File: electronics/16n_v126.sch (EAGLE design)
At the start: 112 parts, among them J1 PJ302M, J10 PJ302M, J11 PJ302M, J12 PJ302M, J13 PJ302M, J14 PJ302M, J15 PJ302M, J16 PJ302M, J2 PJ302M, J3 PJ302M, J4 PJ302M, J5 PJ302M, J6 PJ302M, J7 PJ302M, J8 PJ302M, J9 PJ302M, U1 CD74HC4067SM96, U2 MCP6004_SMD, U3 MCP6004_SMD, U4 MCP6004_SMD, U5 MCP6004_SMD, U6 MCP6004_SMD, U7 MCP6004_SMD, U8 MCP6004_SMD, U9 MCP6004

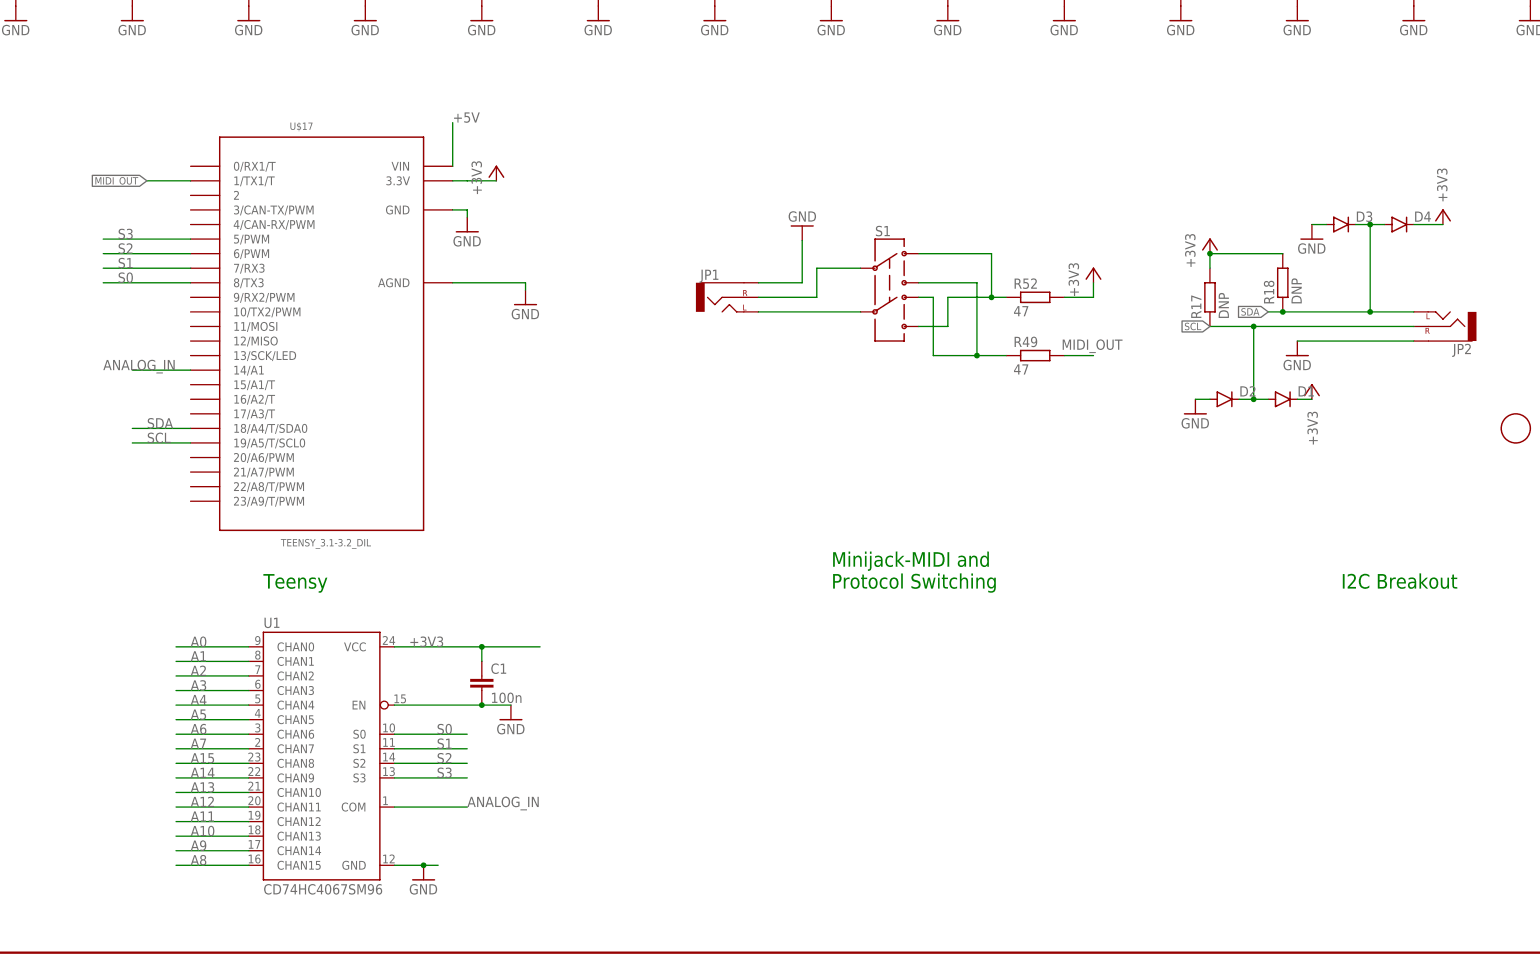
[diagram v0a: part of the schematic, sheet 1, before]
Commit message: 1.26 gets its own files. 1.31 is now the main version.
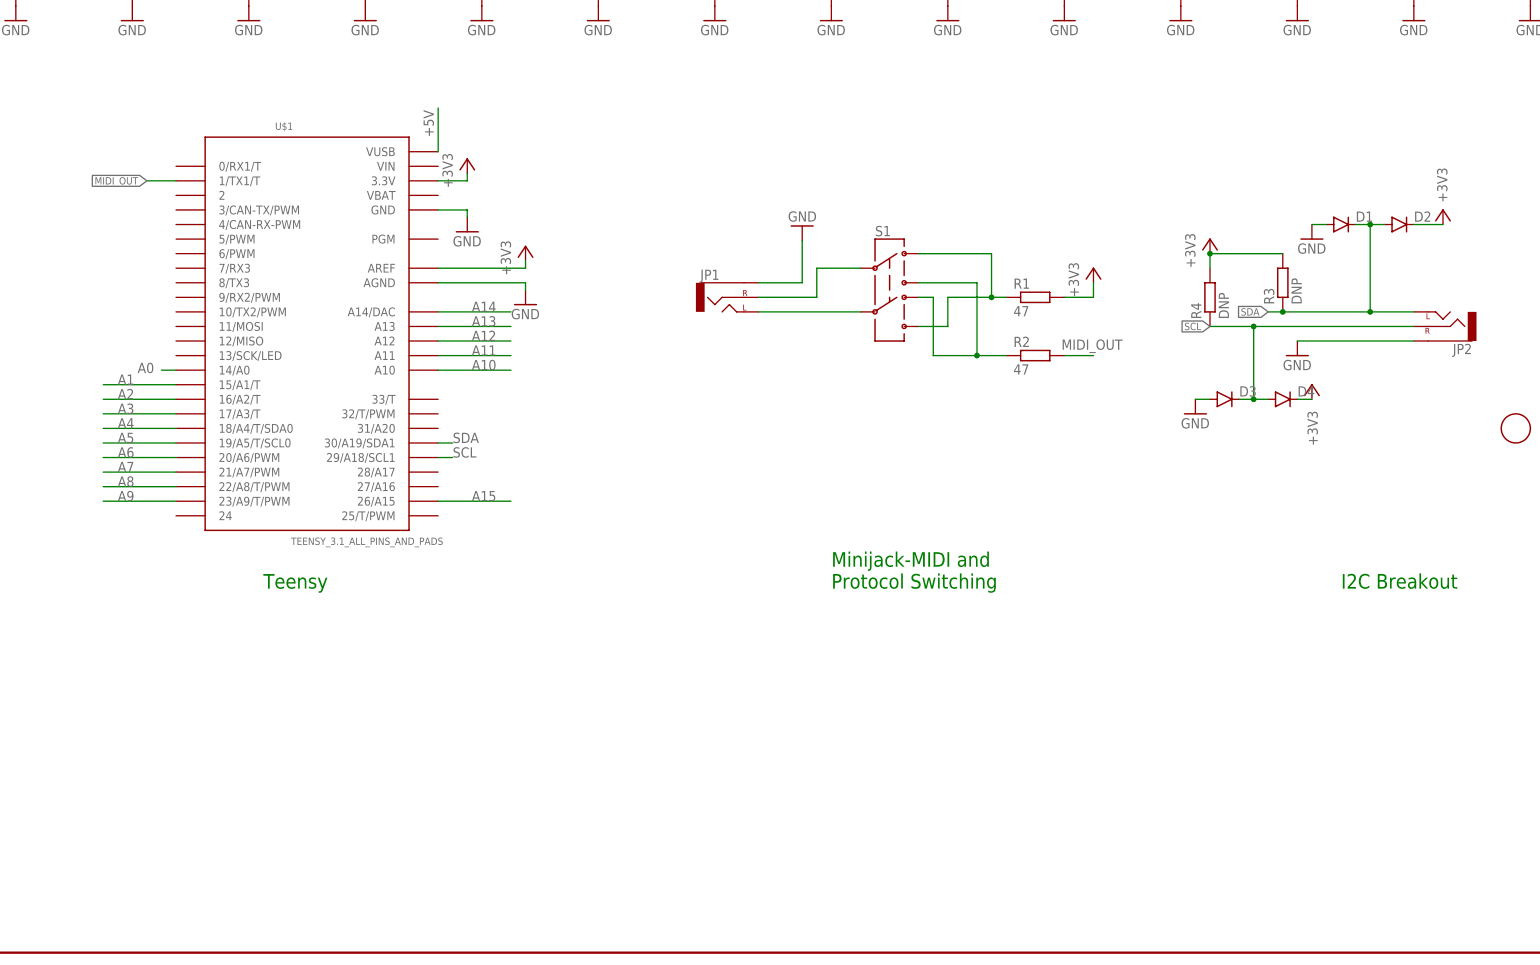
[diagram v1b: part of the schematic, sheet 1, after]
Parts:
- removed C9: 100n, rcl:C-EUC0805
- removed U9: MCP6004, MusicThingModular:MCP6004_SMD
- R1, R2: value 1K -> 47
- R10, R14, R15, R5, R9: value 1K -> 5.6K
- R11, R13, R16, R6, R8: value 1K -> 10K
- R17: value DNP -> 1K
- R18: value DNP -> 10K
- R20, R24, R30, R34, R40, R44: value 10K -> 5.6K
- R21, R23, R31, R33, R41, R43: value 5.6K -> 10K
- R22, R32, R42, R46, R48, R51: value 10K -> 1K
- R27, R37, R45, R47, R50: value 5.6K -> 1K
- R3, R4: value 1K -> DNP
- R49, R52: value 47 -> 1K
- U$1: value SLIDEPOT-ALPS-60MM -> TEENSY_3.1_ALL_PINS_AND_PADS; device monome:SLIDEPOT-ALPS-60MM -> Teensy_3_Series_Board_v1.0:TEENSY_3.1_ALL_PINS_AND_PADS
- U$17: value TEENSY_3.1-3.2_DIL -> SLIDEPOT-ALPS-60MM; device Teensy_3_and_LC_Series_Boards_v1.4:TEENSY_3.1-3.2_DIL -> monome:SLIDEPOT-ALPS-60MM
- U1: value CD74HC4067SM96 -> MCP6004_SMD; device foxfield:744067SO24 -> MusicThingModular:MCP6004_SMD
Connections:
- removed net ANALOG_IN: U$17.14/A1, U1.COM
- removed net S0: U$17.8/TX3, U1.S0
- removed net S1: U$17.7/RX3, U1.S1
- removed net S2: U$17.6/PWM, U1.S2
- removed net S3: U$17.5/PWM, U1.S3
- net +3V3: now also D2.C, R1.2, R3.2, R4.2, U$1.3.3V, U$1.AREF; no longer C1.1, D1.C, R17.2, R18.2, R52.2, U$17.3.3V, U1.VCC
- net +5V: now also C1.1, U$1.VUSB, U$17.1, U1P.V+; no longer C9.1, U$1.1, U$17.VIN, U9P.V+
- net A0: now also U$1.14/A0, U1B.-IN, U1B.OUT; no longer U1.CHAN0, U2B.-IN, U2B.OUT
- net A1: now also U$1.15/A1/T, U1C.-IN, U1C.OUT; no longer U1.CHAN1, U2C.-IN, U2C.OUT
- net A10: now also U$1.A10, U6B.-IN, U6B.OUT; no longer U1.CHAN13, U7B.-IN, U7B.OUT
- net A11: now also U$1.A11, U6C.-IN, U6C.OUT; no longer U1.CHAN12, U7C.-IN, U7C.OUT
- net A12: now also U$1.A12, U7B.-IN, U7B.OUT; no longer U1.CHAN11, U8B.-IN, U8B.OUT
- net A13: now also U$1.A13, U7C.-IN, U7C.OUT; no longer U1.CHAN10, U8C.-IN, U8C.OUT
- net A14: now also U$1.A14/DAC, U8B.-IN, U8B.OUT; no longer U1.CHAN9, U9B.-IN, U9B.OUT
- net A15: now also U$1.26/A15, U8C.-IN, U8C.OUT; no longer U1.CHAN8, U9C.-IN, U9C.OUT
- net A2: now also U$1.16/A2/T, U2B.-IN, U2B.OUT; no longer U1.CHAN2, U3B.-IN, U3B.OUT
- net A3: now also U$1.17/A3/T, U2C.-IN, U2C.OUT; no longer U1.CHAN3, U3C.-IN, U3C.OUT
- net A4: now also U$1.18/A4/T/SDA0, U3B.-IN, U3B.OUT; no longer U1.CHAN4, U4B.-IN, U4B.OUT
- net A5: now also U$1.19/A5/T/SCL0, U3C.-IN, U3C.OUT; no longer U1.CHAN5, U4C.-IN, U4C.OUT
- net A6: now also U$1.20/A6/PWM, U4B.-IN, U4B.OUT; no longer U1.CHAN6, U5B.-IN, U5B.OUT
- net A7: now also U$1.21/A7/PWM, U4C.-IN, U4C.OUT; no longer U1.CHAN7, U5C.-IN, U5C.OUT
- net A8: now also U$1.22/A8/T/PWM, U5B.-IN, U5B.OUT; no longer U1.CHAN15, U6B.-IN, U6B.OUT
- net A9: now also U$1.23/A9/T/PWM, U5C.-IN, U5C.OUT; no longer U1.CHAN14, U6C.-IN, U6C.OUT
- net CV1: now also R7.2; no longer R1.2
- net CV10: now also R48.2; no longer R10.2
- net CV11: now also R32.2; no longer R11.2
- net CV12: now also R49.2; no longer R12.2
- net CV13: now also R37.2; no longer R13.2
- net CV14: now also R50.2; no longer R14.2
- net CV15: now also R42.2; no longer R15.2
- net CV16: now also R51.2; no longer R16.2
- net CV2: now also R12.2; no longer R2.2
- net CV3: now also R52.2; no longer R3.2
- net CV4: now also R45.2; no longer R4.2
- net CV5: now also R17.2; no longer R5.2
- net CV6: now also R47.2; no longer R6.2
- net CV7: now also R22.2; no longer R7.2
- net CV8: now also R46.2; no longer R8.2
- net CV9: now also R27.2; no longer R9.2
- net GND: now also D1.A, R11.1, R13.1, R16.1, R18.1, R21.1, R23.1, R31.1, R33.1, R41.1, R43.1, R6.1, R8.1, U$1.AGND, U$1.GND, U$17.3, U1P.V-; no longer C9.2, D2.A, R20.1, R22.1, R24.1, R30.1, R32.1, R34.1, R40.1, R42.1, R44.1, R46.1, R48.1, R51.1, U$1.3, U$17.AGND, U$17.GND, U1.EN, U1.GND, U9P.V-
- net MIDI_OUT: now also R2.2, U$1.1/TX1/T; no longer R49.2, U$17.1/TX1/T
- net N$10: now also R8.2, R9.2, U1C.+IN; no longer R21.2, R22.2, U2C.+IN
- net N$12: now also R15.2, R16.2, U3B.+IN; no longer R39.2, R40.2, U4B.+IN
- net N$13: now also R18.2, R19.2, U3C.+IN; no longer R25.2, R26.2, U4C.+IN
- net N$15: now also R20.2, R21.2, U4B.+IN; no longer R41.2, R42.2, U5B.+IN
- net N$16: now also R23.2, R24.2, U4C.+IN; no longer R27.2, R28.2, U5C.+IN
- net N$18: now also R25.2, R26.2, U5B.+IN; no longer R43.2, R44.2, U6B.+IN
- net N$19: now also R28.2, U5C.+IN; no longer R30.2, U6C.+IN
- net N$21: now also R30.2, R31.2, U6B.+IN; no longer R45.2, R46.2, U7B.+IN
- net N$22: now also R33.2, R34.2, U6C.+IN; no longer R31.2, R32.2, U7C.+IN
- net N$24: now also R35.2, R36.2, U7B.+IN; no longer R47.2, R48.2, U8B.+IN
- net N$25: now also R38.2, R39.2, U7C.+IN; no longer R33.2, R34.2, U8C.+IN
- net N$27: now also R40.2, R41.2, U8B.+IN; no longer R50.2, R51.2, U9B.+IN
- net N$28: now also R43.2, R44.2, U8C.+IN; no longer R19.2, R20.2, U9C.+IN
- net N$3: now also R2.1; no longer R49.1
- net N$300: now also R7.1, U1A.-IN, U1A.OUT; no longer R1.1, U2A.-IN, U2A.OUT
- net N$301: now also R12.1, U1D.-IN, U1D.OUT; no longer R2.1, U2D.-IN, U2D.OUT
- net N$302: now also R52.1, U2A.-IN, U2A.OUT; no longer R3.1, U3A.-IN, U3A.OUT
- net N$303: now also R45.1, U2D.-IN, U2D.OUT; no longer R4.1, U3D.-IN, U3D.OUT
- net N$304: now also R17.1, U3A.-IN, U3A.OUT; no longer R5.1, U4A.-IN, U4A.OUT
- net N$305: now also R47.1, U3D.-IN, U3D.OUT; no longer R6.1, U4D.-IN, U4D.OUT
- net N$306: now also R22.1, U4A.-IN, U4A.OUT; no longer R7.1, U5A.-IN, U5A.OUT
- net N$307: now also R46.1, U4D.-IN, U4D.OUT; no longer R8.1, U5D.-IN, U5D.OUT
- net N$308: now also R27.1, U5A.-IN, U5A.OUT; no longer R9.1, U6A.-IN, U6A.OUT
- net N$309: now also R48.1, U5D.-IN, U5D.OUT; no longer R10.1, U6D.-IN, U6D.OUT
- net N$310: now also R32.1, U6A.-IN, U6A.OUT; no longer R11.1, U7A.-IN, U7A.OUT
- net N$311: now also R49.1, U6D.-IN, U6D.OUT; no longer R12.1, U7D.-IN, U7D.OUT
- net N$312: now also R37.1, U7A.-IN, U7A.OUT; no longer R13.1, U8A.-IN, U8A.OUT
- net N$313: now also R50.1, U7D.-IN, U7D.OUT; no longer R14.1, U8D.-IN, U8D.OUT
- net N$314: now also R42.1, U8A.-IN, U8A.OUT; no longer R15.1, U9A.-IN, U9A.OUT
- net N$315: now also R51.1, U8D.-IN, U8D.OUT; no longer R16.1, U9D.-IN, U9D.OUT
- net N$4: now also R1.1; no longer R52.1
- net N$6: now also R10.2, R11.2, U2B.+IN; no longer R37.2, R38.2, U3B.+IN
- net N$7: now also R13.2, R14.2, U2C.+IN; no longer R23.2, R24.2, U3C.+IN
- net N$9: now also R5.2, R6.2, U1B.+IN; no longer R35.2, R36.2, U2B.+IN
- net SCL: now also D3.C, D4.A, R4.1, U$1.29/A18/SCL1; no longer D1.A, D2.C, R17.1, U$17.19/A5/T/SCL0
- net SDA: now also D1.C, D2.A, R3.1, U$1.30/A19/SDA1; no longer D3.C, D4.A, R18.1, U$17.18/A4/T/SDA0
- net W0: now also R5.1, U$17.2, U1A.+IN; no longer R35.1, U$1.2, U2A.+IN
- net W1: now also R9.1, U$16.2, U1D.+IN; no longer R21.1, U$2.2, U2D.+IN
- net W10: now also R30.1, U$7.2, U6A.+IN; no longer R45.1, U$11.2, U7A.+IN
- net W11: now also R34.1, U$6.2, U6D.+IN; no longer R31.1, U$12.2, U7D.+IN
- net W12: now also R35.1, U$5.2, U7A.+IN; no longer R47.1, U$13.2, U8A.+IN
- net W13: now also R39.1, U$4.2, U7D.+IN; no longer R33.1, U$14.2, U8D.+IN
- net W14: now also R40.1, U$3.2, U8A.+IN; no longer R50.1, U$15.2, U9A.+IN
- net W15: now also R44.1, U$2.2, U8D.+IN; no longer R19.1, U$16.2, U9D.+IN
- net W2: now also R10.1, U$15.2, U2A.+IN; no longer R37.1, U$3.2, U3A.+IN
- net W3: now also R14.1, U$14.2, U2D.+IN; no longer R23.1, U$4.2, U3D.+IN
- net W4: now also R15.1, U$13.2, U3A.+IN; no longer R39.1, U$5.2, U4A.+IN
- net W5: now also R19.1, U$12.2, U3D.+IN; no longer R25.1, U$6.2, U4D.+IN
- net W6: now also R20.1, U$11.2, U4A.+IN; no longer R41.1, U$7.2, U5A.+IN
- net W7: now also R24.1, U$10.2, U4D.+IN; no longer R27.1, U$8.2, U5D.+IN
- net W8: now also R25.1, U5A.+IN; no longer R43.1, U6A.+IN
- net W9: now also U$8.2, U5D.+IN; no longer U$10.2, U6D.+IN
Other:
- moved on the sheet: C2, C3, C4, C5, C6, C7, C8, D1, D2, D3, D4, R10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
